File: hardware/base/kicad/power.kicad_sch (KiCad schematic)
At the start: 54 parts, among them J1 POWER, J2 USB micro-B, Q11 AO3401A, U1 TPS54360BDDAR, U2 TPD4E05U06DQAR, U3 TPS62A02ADRLR

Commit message: VBUS on the outer channel of U2, Tag-Connect at the SWD corner, V3IN at 0.3 mm in the complete pass
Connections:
- net VBUS: now also U2.5 (D2-), U2.6 (NC); no longer U2.4 (D2+), U2.7 (NC)

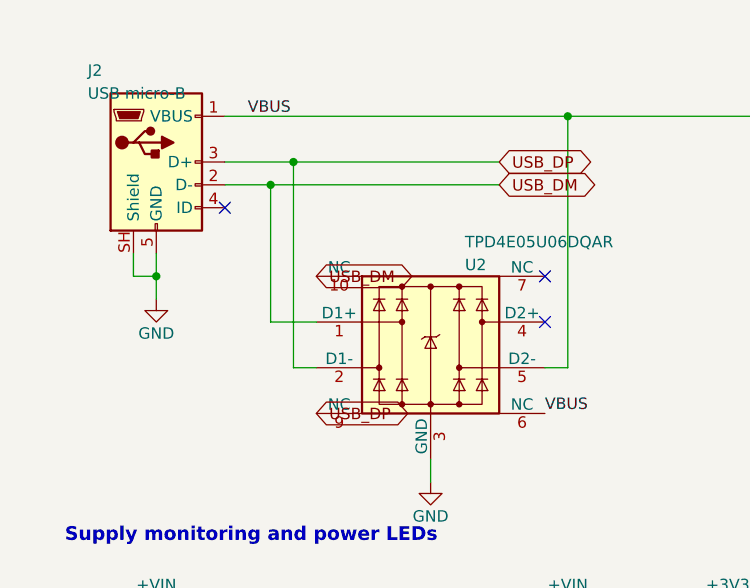
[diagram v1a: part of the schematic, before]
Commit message: USB_DP on the ESD channel nearer its MCU pin: the pair flows through U2 without crossing
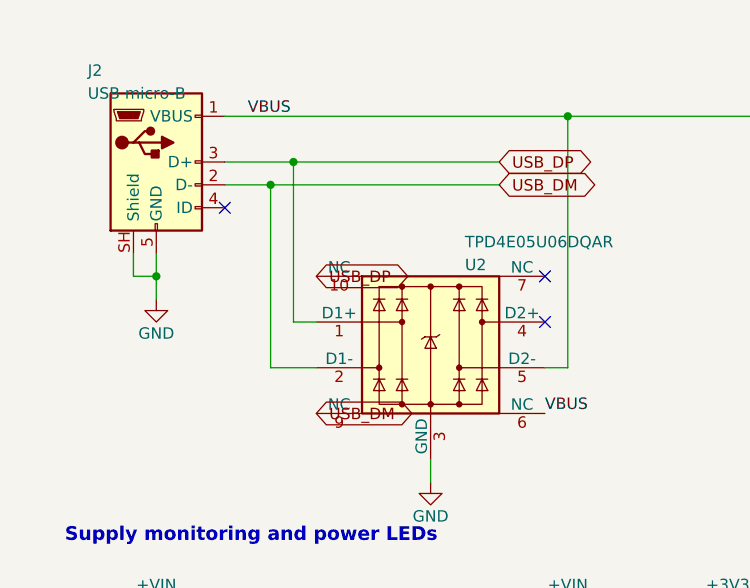
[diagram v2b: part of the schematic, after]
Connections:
- net USB_DM: now also U2.2 (D1-), U2.9 (NC); no longer U2.1 (D1+), U2.10 (NC)
- net USB_DP: now also U2.1 (D1+), U2.10 (NC); no longer U2.2 (D1-), U2.9 (NC)

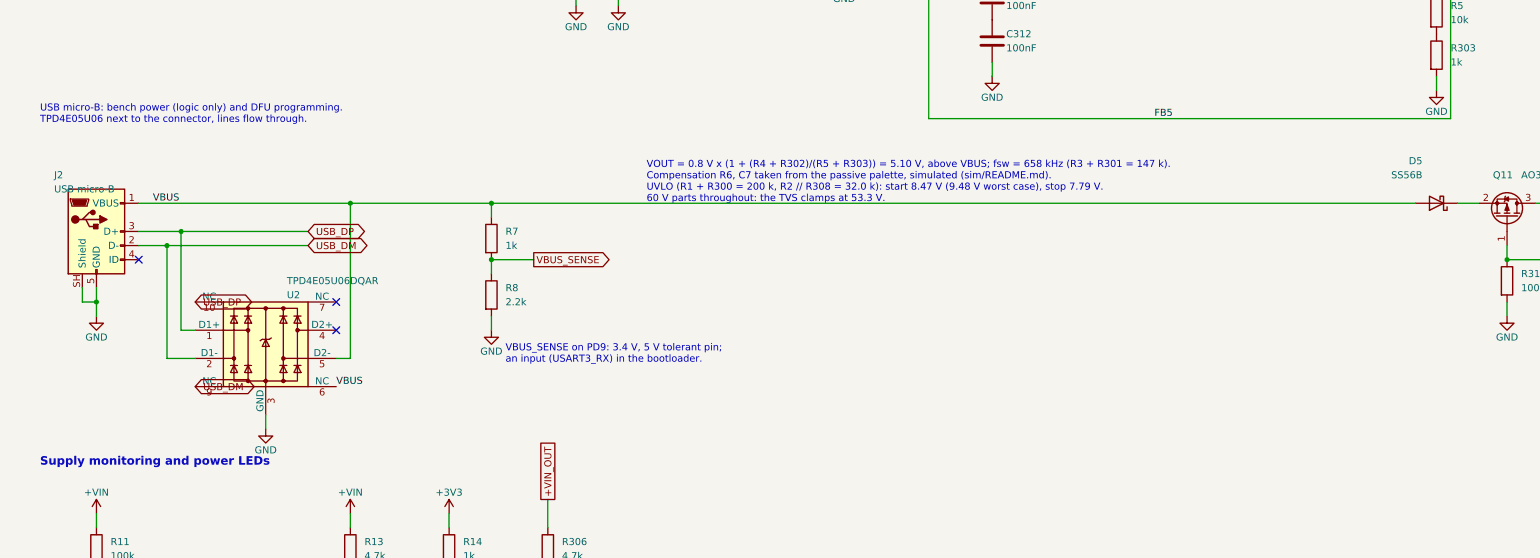
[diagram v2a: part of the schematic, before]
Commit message: USB jack, its ESD and VBUS sense on the MCU sheet; channel and block checks; renet and unroute of the working board
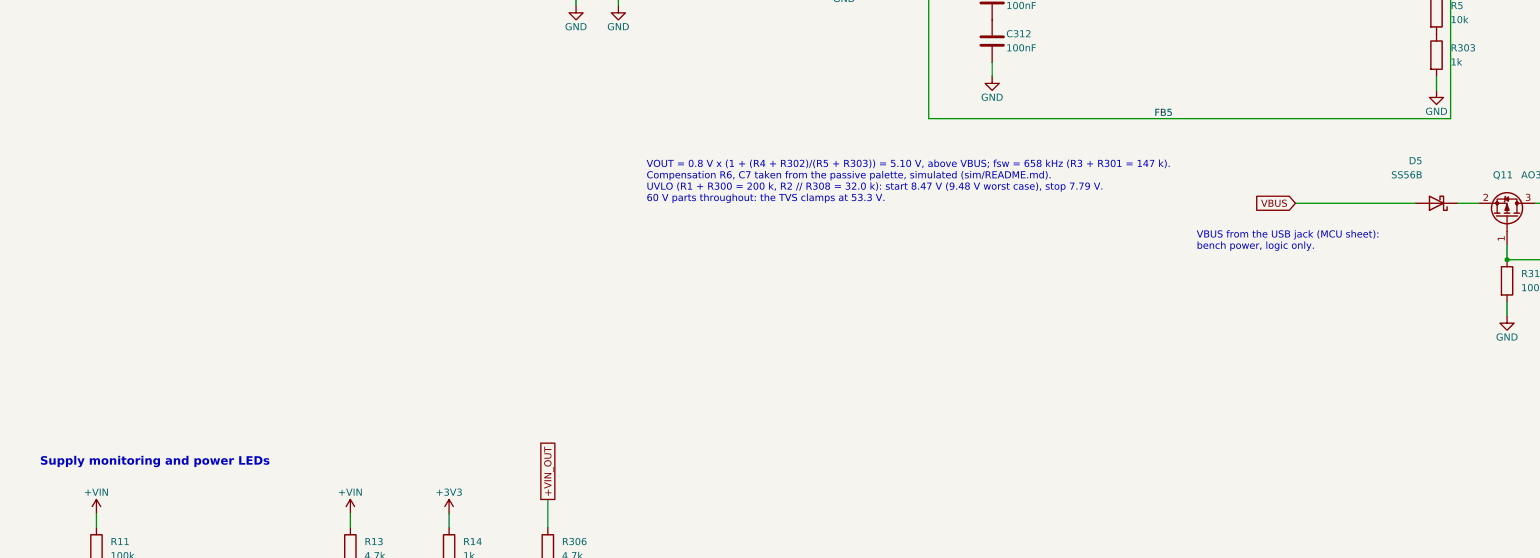
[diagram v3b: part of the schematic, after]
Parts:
- removed J2: USB micro-B, Connector_USB:USB_Micro-B_Molex-105133-0001, symbol Connector:USB_B_Micro
- removed R7: 1k, Resistor_SMD:R_0402_1005Metric, symbol Device:R
- removed R8: 2.2k, Resistor_SMD:R_0402_1005Metric, symbol Device:R
- removed U2: TPD4E05U06DQAR, Package_SON:USON-10_2.5x1.0mm_P0.5mm, symbol Power_Protection:TPD4E05U06DQA
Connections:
- no-connect marks 5 -> 2
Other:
- note added: "VBUS from the USB jack (MCU sheet): bench power, logic only."
- note removed: "USB micro-B: bench power (logic only) and DFU programming. TPD4E05U06 next to the connector, lines flow through."
- note removed: "VBUS_SENSE on PD9: 3.4 V, 5 V tolerant pin; an input (USART3_RX) in the bootloader."
- title: 12 or 24 V input, 5 V and 3.3 V bucks, USB -> 12 or 24 V input, 5 V and 3.3 V bucks, USB VBUS
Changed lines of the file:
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@@
 	(paper "A3")
 	(title_block
-		(title "12 or 24 V input, 5 V and 3.3 V bucks, USB")
+		(title "12 or 24 V input, 5 V and 3.3 V bucks, USB VBUS")
 		(date "2026-10-18")
 		(rev "A")
